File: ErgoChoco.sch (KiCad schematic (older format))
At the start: 145 parts, among them J1 USB_B_Micro, Q1 Q_NPN_BCE, SW1 SW_Push, U1 ATmega32U4-AU, U2 PRTR5V0U2X, Y1 16MHz

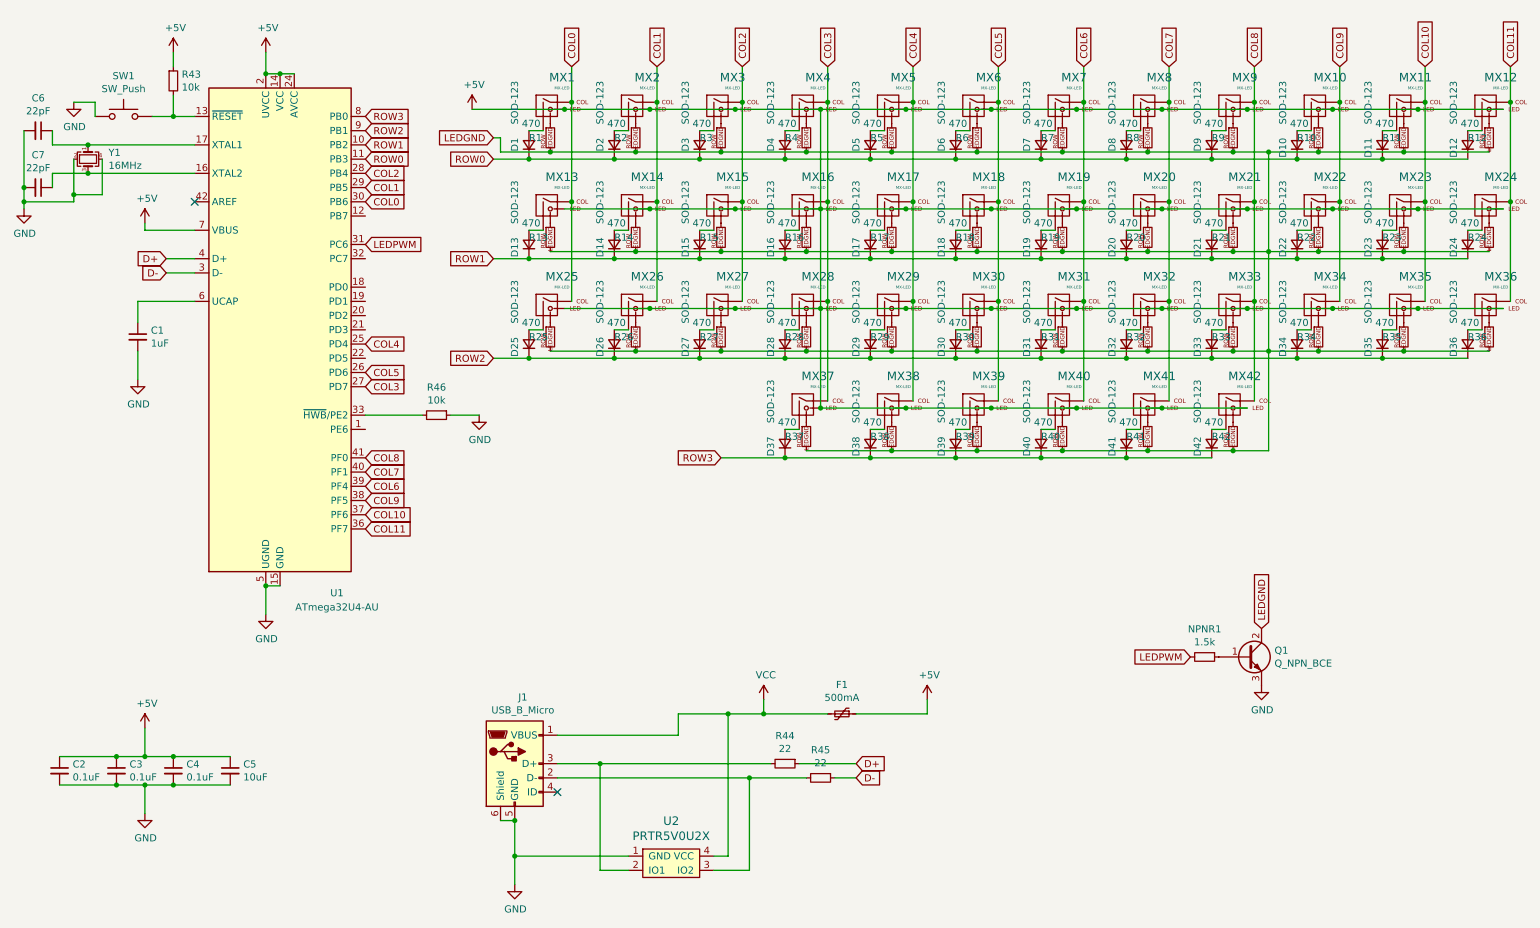
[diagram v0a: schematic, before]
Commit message: deleted old schematic for atmega32u4 also
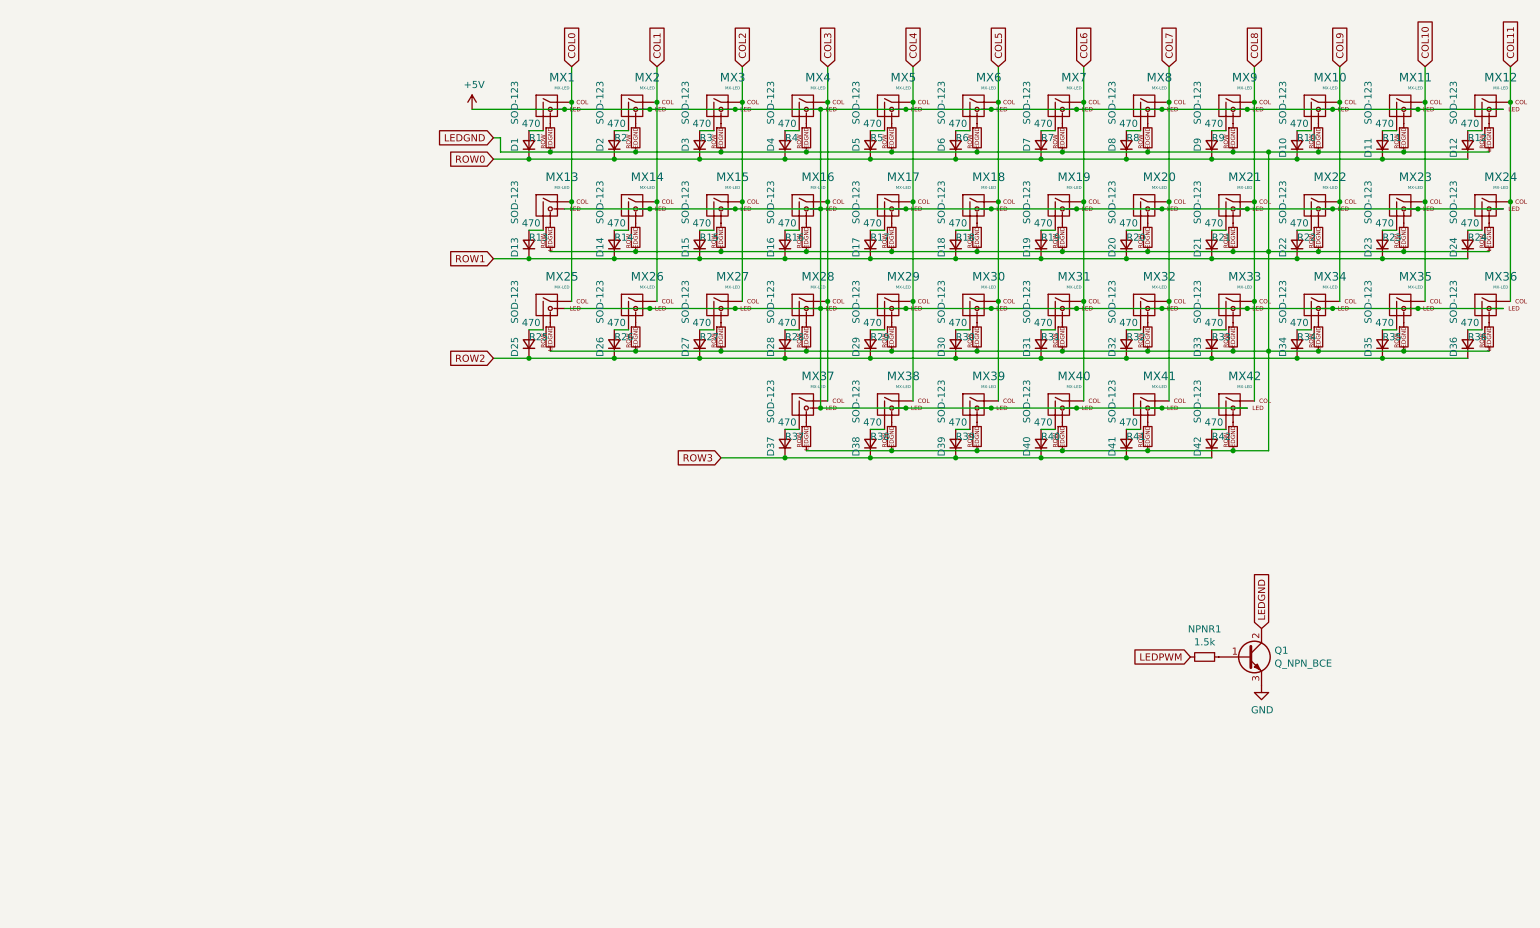
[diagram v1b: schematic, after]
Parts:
- removed C1: 1uF, Capacitor_SMD:C_0805_2012Metric, symbol Device:C_Small
- removed C2, C3, C4: 0.1uF, Capacitor_SMD:C_0805_2012Metric, symbol Device:C_Small
- removed C5: 10uF, Capacitor_SMD:C_0805_2012Metric, symbol Device:C_Small
- removed C6, C7: 22pF, Capacitor_SMD:C_0805_2012Metric, symbol Device:C_Small
- removed F1: 500mA, Fuse:Fuse_1206_3216Metric, symbol Device:Polyfuse_Small
- removed J1: USB_B_Micro, Choco617_parts:CUI_UJ2-MIBH2-4-SMT, symbol Connector:USB_B_Micro
- removed R43, R46: 10k, Resistor_SMD:R_0805_2012Metric, symbol Device:R_Small
- removed R44, R45: 22, Resistor_SMD:R_0805_2012Metric, symbol Device:R_Small
- removed SW1: SW_Push, random-keyboard-parts:SKQG-1155865, symbol Switch:SW_Push
- removed U1: ATmega32U4-AU, Package_QFP:TQFP-44_10x10mm_P0.8mm, symbol MCU_Microchip_ATmega:ATmega32U4-AU
- removed U2: PRTR5V0U2X, random-keyboard-parts:SOT143B, symbol random-keyboard-parts:PRTR5V0U2X
- removed Y1: 16MHz, Crystal:Crystal_SMD_3225-4Pin_3.2x2.5mm, symbol Device:Crystal_GND24_Small
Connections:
- no-connect marks 2 -> 0

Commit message: introduced Pro Micro
-put Pro Micro into schematic
-updated PCB from schematic
-moved all switches 10mm farther apart
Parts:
- added U1: ProMicro, Keebio-Parts:ArduinoProMicro, symbol keebio:ProMicro
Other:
- moved on the sheet: D1, D10, D11, D12, D13, D14, D15, D16, D17, D18, D19, D2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

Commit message: routed other two LH rows
-still excluding innermost row and thumb cluster for now
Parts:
- D1, D10, D11, D12, D13, D14, D15, D16, D17, D18, D19, D2, D20, D21, D22, D23, D24, D25, D26, D27, D28, D29, D3, D30, D31, D32, D33, D34, D35, D36, D37, D38, D39, D4, D40, D41, D42, D5, D6, D7, D8, D9: footprint Diode_SMD:D_SOD-123 -> Choco617_parts:D_SOD-123-HandSolder

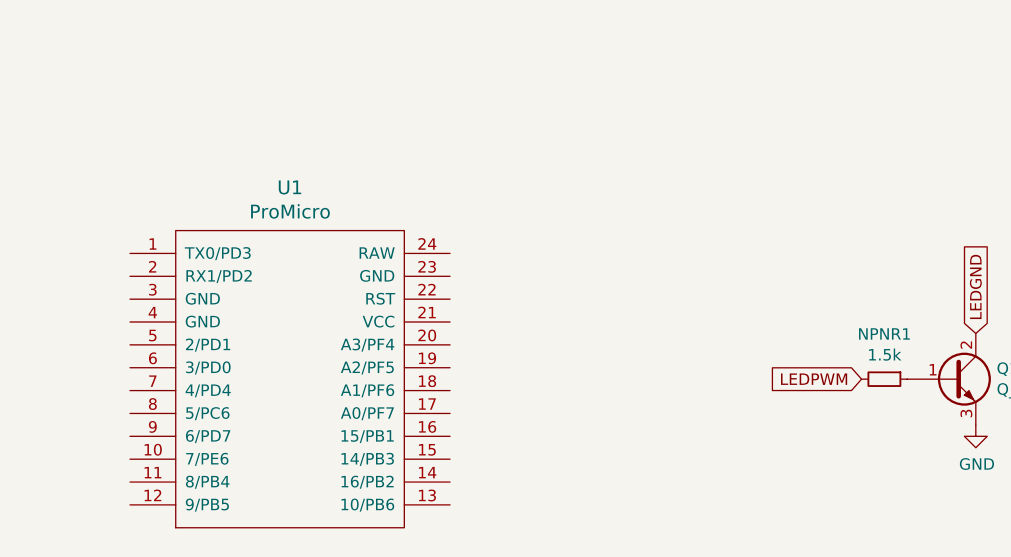
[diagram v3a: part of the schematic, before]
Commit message: finished routing, added mounting holes
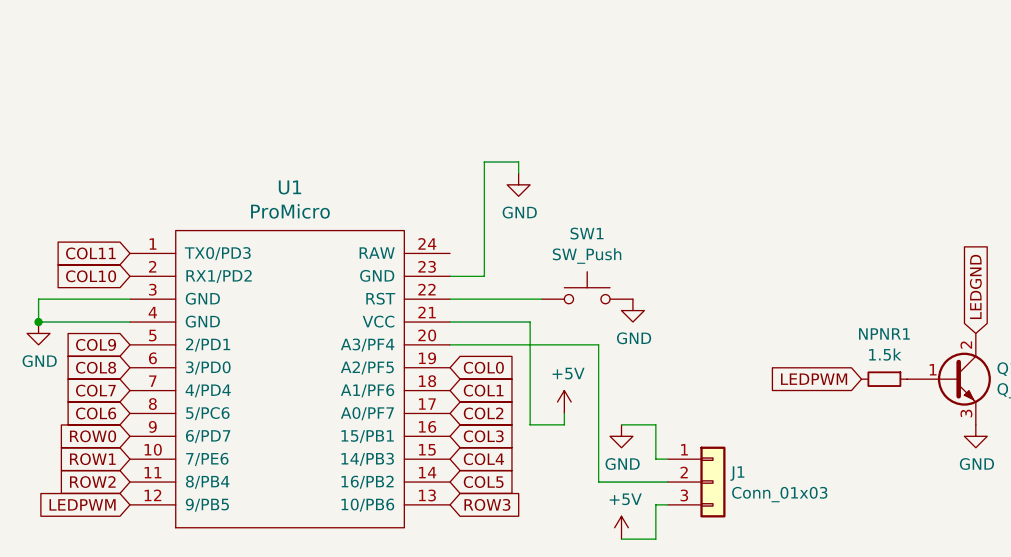
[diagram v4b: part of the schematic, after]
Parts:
- added J1: Conn_01x03, Connector_PinHeader_2.54mm:PinHeader_1x03_P2.54mm_Vertical, symbol Connector_Generic:Conn_01x03
- added SW1: SW_Push, random-keyboard-parts:SKQG-1155865, symbol Switch:SW_Push
- Q1: footprint digikey-footprints:Trans_SOT-223-4 -> digikey-footprints:SOT-23-3
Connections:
- net +5V: now also U1.21 (VCC), J1.3 (Pin_3)
- net COL0: now also U1.19 (A2/PF5)
- net COL1: now also U1.18 (A1/PF6)
- net COL10: now also U1.2 (RX1/PD2)
- net COL11: now also U1.1 (TX0/PD3)
- net COL2: now also U1.17 (A0/PF7)
- net COL3: now also U1.16 (15/PB1)
- net COL4: now also U1.15 (14/PB3)
- net COL5: now also U1.14 (16/PB2)
- net COL6: now also U1.8 (5/PC6)
- net COL7: now also U1.7 (4/PD4)
- net COL8: now also U1.6 (3/PD0)
- net COL9: now also U1.5 (2/PD1)
- net GND: now also U1.23 (GND), U1.3 (GND), U1.4 (GND), J1.1 (Pin_1), SW1.2
- net LEDPWM: now also U1.12 (9/PB5)
- net ROW0: now also U1.9 (6/PD7)
- net ROW1: now also U1.10 (7/PE6)
- net ROW2: now also U1.11 (8/PB4)
- net ROW3: now also U1.13 (10/PB6)
- net at U1.20 (A3/PF4): now also J1.2 (Pin_2)
- net at U1.22 (RST): now also SW1.1
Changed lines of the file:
@@
 F 0 "Q1" H 5791 5746 50  0000 L CNN
 F 1 "Q_NPN_BCE" H 5791 5655 50  0000 L CNN
-F 2 "digikey-footprints:Trans_SOT-223-4" H 5800 5800 50  0001 C CNN
+F 2 "digikey-footprints:SOT-23-3" H 5800 5800 50  0001 C CNN
 F 3 "~" H 5600 5700 50  0001 C CNN
 	1    5600 5700
@@
 	1    0    0    -1
 $EndComp
+$Comp
+L Switch:SW_Push SW1
+U 1 1 5F134FD2
+P 4000 5350
+F 0 "SW1" H 4000 5635 50  0000 C CNN
+F 1 "SW_Push" H 4000 5544 50  0000 C CNN
+F 2 "random-keyboard-parts:SKQG-1155865" H 4000 5550 50  0001 C CNN
+F 3 "~" H 4000 5550 50  0001 C CNN
+	1    4000 5350
+	1    0    0    -1
+$EndComp
+Wire Wire Line
+	3400 5350 3800 5350
+$Comp
+L power:GND #PWR0101
+U 1 1 5F1466C9
+P 4200 5350
+F 0 "#PWR0101" H 4200 5100 50  0001 C CNN
+F 1 "GND" H 4205 5177 50  0000 C CNN
+F 2 "" H 4200 5350 50  0001 C CNN
+F 3 "" H 4200 5350 50  0001 C CNN
+	1    4200 5350
+	1    0    0    -1
+$EndComp
+Text GLabel 2000 5950 0    50   Input ~ 0
+ROW0
+Text GLabel 2000 6050 0    50   Input ~ 0
+ROW1
+Text GLabel 2000 6150 0    50   Input ~ 0
+ROW2
+Text GLabel 3400 6250 2    50   Input ~ 0
+ROW3
+Text GLabel 3400 5650 2    50   Input ~ 0
+COL0
+Text GLabel 3400 5750 2    50   Input ~ 0
+COL1
+Text GLabel 3400 5850 2    50   Input ~ 0
+COL2
+Text GLabel 3400 5950 2    50   Input ~ 0
+COL3
+Text GLabel 3400 6050 2    50   Input ~ 0
+COL4
+Text GLabel 3400 6150 2    50   Input ~ 0
+COL5
+Text GLabel 2000 5850 0    50   Input ~ 0
+COL6
+Text GLabel 2000 5750 0    50   Input ~ 0
+COL7
+Text GLabel 2000 5650 0    50   Input ~ 0
+COL8
+Text GLabel 2000 5550 0    50   Input ~ 0
+COL9
+Text GLabel 2000 5250 0    50   Input ~ 0
+COL10
+Text GLabel 2000 5150 0    50   Input ~ 0
+COL11
+$Comp
+L power:GND #PWR0102
+U 1 1 5F145398
+P 1600 5450
+F 0 "#PWR0102" H 1600 5200 50  0001 C CNN
+F 1 "GND" H 1605 5277 50  0000 C CNN
+F 2 "" H 1600 5450 50  0001 C CNN
+F 3 "" H 1600 5450 50  0001 C CNN
+	1    1600 5450
+	1    0    0    -1
+$EndComp
+Wire Wire Line
+	2000 5350 1600 5350
+Wire Wire Line
+	1600 5350 1600 5450
+Wire Wire Line
+	2000 5450 1600 5450
+Connection ~ 1600 5450
+$Comp
+L power:GND #PWR0103
+U 1 1 5F169795
+P 3700 4800
+F 0 "#PWR0103" H 3700 4550 50  0001 C CNN
+F 1 "GND" H 3705 4627 50  0000 C CNN
+F 2 "" H 3700 4800 50  0001 C CNN
+F 3 "" H 3700 4800 50  0001 C CNN
+	1    3700 4800
+	1    0    0    -1
+$EndComp
+Wire Wire Line
+	3400 5250 3550 5250
+Wire Wire Line
+	3550 5250 3550 4750
+Wire Wire Line
+	3550 4750 3700 4750
+Wire Wire Line
+	3700 4750 3700 4800
+$Comp
+L power:+5V #PWR0104
+U 1 1 5F17C12B
+P 3900 5850
+F 0 "#PWR0104" H 3900 5700 50  0001 C CNN
+F 1 "+5V" H 3915 6023 50  0000 C CNN
+F 2 "" H 3900 5850 50  0001 C CNN
+F 3 "" H 3900 5850 50  0001 C CNN
+	1    3900 5850
+	1    0    0    -1
+$EndComp
+Wire Wire Line
+	3400 5450 3750 5450
+Wire Wire Line
+	3750 5450 3750 5900
+Wire Wire Line
+	3750 5900 3900 5900
+Wire Wire Line
+	3900 5900 3900 5850
+Text GLabel 2000 6250 0    50   Input ~ 0
+LEDPWM
+$Comp
+L Connector_Generic:Conn_01x03 J1
+U 1 1 5F15B661
+P 4550 6150
+F 0 "J1" H 4630 6192 50  0000 L CNN
+F 1 "Conn_01x03" H 4630 6101 50  0000 L CNN
+F 2 "Connector_PinHeader_2.54mm:PinHeader_1x03_P2.54mm_Vertical" H 4550 6150 50  0001 C CNN
+F 3 "~" H 4550 6150 50  0001 C CNN
+	1    4550 6150
+	1    0    0    -1
+$EndComp
+$Comp
+L power:GND #PWR0105
+U 1 1 5F16FC44
+P 4150 5900
+F 0 "#PWR0105" H 4150 5650 50  0001 C CNN
+F 1 "GND" H 4155 5727 50  0000 C CNN
+F 2 "" H 4150 5900 50  0001 C CNN
+F 3 "" H 4150 5900 50  0001 C CNN
+	1    4150 5900
+	1    0    0    -1
+$EndComp
+$Comp
+L power:+5V #PWR0106
+U 1 1 5F17076B
+P 4150 6400
+F 0 "#PWR0106" H 4150 6250 50  0001 C CNN
+F 1 "+5V" H 4165 6573 50  0000 C CNN
+F 2 "" H 4150 6400 50  0001 C CNN
+F 3 "" H 4150 6400 50  0001 C CNN
+	1    4150 6400
+	1    0    0    -1
+$EndComp
+Wire Wire Line
+	4350 6250 4300 6250
+Wire Wire Line
+	4300 6250 4300 6400
+Wire Wire Line
+	4300 6400 4150 6400
+Wire Wire Line
+	4350 6050 4300 6050
+Wire Wire Line
+	4300 6050 4300 5900
+Wire Wire Line
+	4300 5900 4150 5900
+Wire Wire Line
+	3400 5550 4050 5550
+Wire Wire Line
+	4050 5550 4050 6150
+Wire Wire Line
+	4050 6150 4350 6150
 $EndSCHEMATC
